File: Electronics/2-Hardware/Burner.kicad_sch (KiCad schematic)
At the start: 9 parts, among them P3 CONN_1, P6 CONN_1, Q1 Q_NMOS_DGS, U2 LM317_TO-220, U3 LM317_TO-220

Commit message: Update to KiCad
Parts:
- added D1: PMEG3010ER, Diode_SMD:Nexperia_CFP3_SOD-123W, symbol Diode:PMEG3010ER
- BT1: footprint (none) -> Battery:BatteryHolder_Keystone_1042_1x18650
- Q1: footprint (none) -> Package_TO_SOT_SMD:SOT-23
- R1: footprint ~ -> Battery:BatteryHolder_Keystone_1042_1x18650
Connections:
- net at U1.14 (5V): no longer U2.2 (VO)
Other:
- company: (none) -> Make to Innovate
- title: (none) -> HABET Burner Board - Nero
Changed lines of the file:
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@@
   (paper "A4")
   (title_block
-    (date "26 mar 2014")
+    (title "HABET Burner Board - Nero")
+    (date "2023-07-08")
+    (rev "2")
+    (company "Make to Innovate")
+    (comment 1 "Matthew E. Nelson")
   )
   (junction (at 78.74 148.59) (diameter 0) (color 0 0 0 0)
@@
   )
   (wire (pts (xy 88.9 76.2) (xy 97.79 76.2))
-    (stroke (width 0) (type default))
-  )
-  (wire (pts (xy 97.79 76.2) (xy 97.79 97.79))
     (stroke (width 0) (type default))
   )
@@
     )
     (property "Footprint" "~" (at 86.36 150.368 90)
-      (effects (font (size 0.762 0.762)))
+      (effects (font (size 0.762 0.762)) hide)
     )
     (property "Datasheet" "~" (at 86.36 148.59 0)
@@
       (effects (font (size 1.016 1.016)))
     )
-    (property "Footprint" "~" (at 52.832 161.29 90)
-      (effects (font (size 0.762 0.762)))
+    (property "Footprint" "Battery:BatteryHolder_Keystone_1042_1x18650" (at 52.832 161.29 90)
+      (effects (font (size 0.762 0.762)) hide)
     )
     (property "Datasheet" "~" (at 54.61 161.29 0)
@@
     )
     (property "Footprint" "~" (at 102.87 156.21 0)
-      (effects (font (size 1.524 1.524)))
+      (effects (font (size 1.524 1.524)) hide)
     )
     (property "Datasheet" "~" (at 102.87 156.21 0)
@@
     )
     (property "Footprint" "~" (at 102.87 161.29 0)
-      (effects (font (size 1.524 1.524)))
+      (effects (font (size 1.524 1.524)) hide)
     )
     (property "Datasheet" "~" (at 102.87 161.29 0)
@@
         (path "/ef9e4c29-e04e-4025-8830-037b9cad2048"
           (reference "P6") (unit 1)
+        )
+      )
+    )
+  )
+  (symbol (lib_id "Diode:PMEG3010ER") (at 102.87 87.63 90) (unit 1)
+    (in_bom yes) (on_board yes) (dnp no) (fields_autoplaced)
+    (property "Reference" "D1" (at 105.41 87.3125 90)
+      (effects (font (size 1.27 1.27)) (justify right))
+    )
+    (property "Value" "PMEG3010ER" (at 105.41 89.8525 90)
+      (effects (font (size 1.27 1.27)) (justify right))
+    )
+    (property "Footprint" "Diode_SMD:Nexperia_CFP3_SOD-123W" (at 107.315 87.63 0)
+      (effects (font (size 1.27 1.27)) hide)
+    )
+    (property "Datasheet" "https://assets.nexperia.com/documents/data-sheet/PMEG3010ER.pdf" (at 102.87 87.63 0)
+      (effects (font (size 1.27 1.27)) hide)
+    )
+    (pin "1")
+    (pin "2")
+    (instances
+      (project "Burner"
+        (path "/ef9e4c29-e04e-4025-8830-037b9cad2048"
+          (reference "D1") (unit 1)
         )
       )
@@
       (effects (font (size 1.27 1.27)) (justify left))
     )
-    (property "Footprint" "" (at 99.06 167.64 0)
+    (property "Footprint" "Package_TO_SOT_SMD:SOT-23" (at 99.06 167.64 0)
       (effects (font (size 1.27 1.27)) hide)
     )
@@
       (effects (font (size 1.27 1.27)) (justify left))
     )
-    (property "Footprint" "" (at 57.15 37.846 90)
-      (effects (font (size 1.27 1.27)) hide)
-    )
+    (property "Footprint" "Battery:BatteryHolder_Keystone_1042_1x18650" (at 57.15 37.846 90)
+      (effects (font (size 1.27 1.27)) hide)
+    )

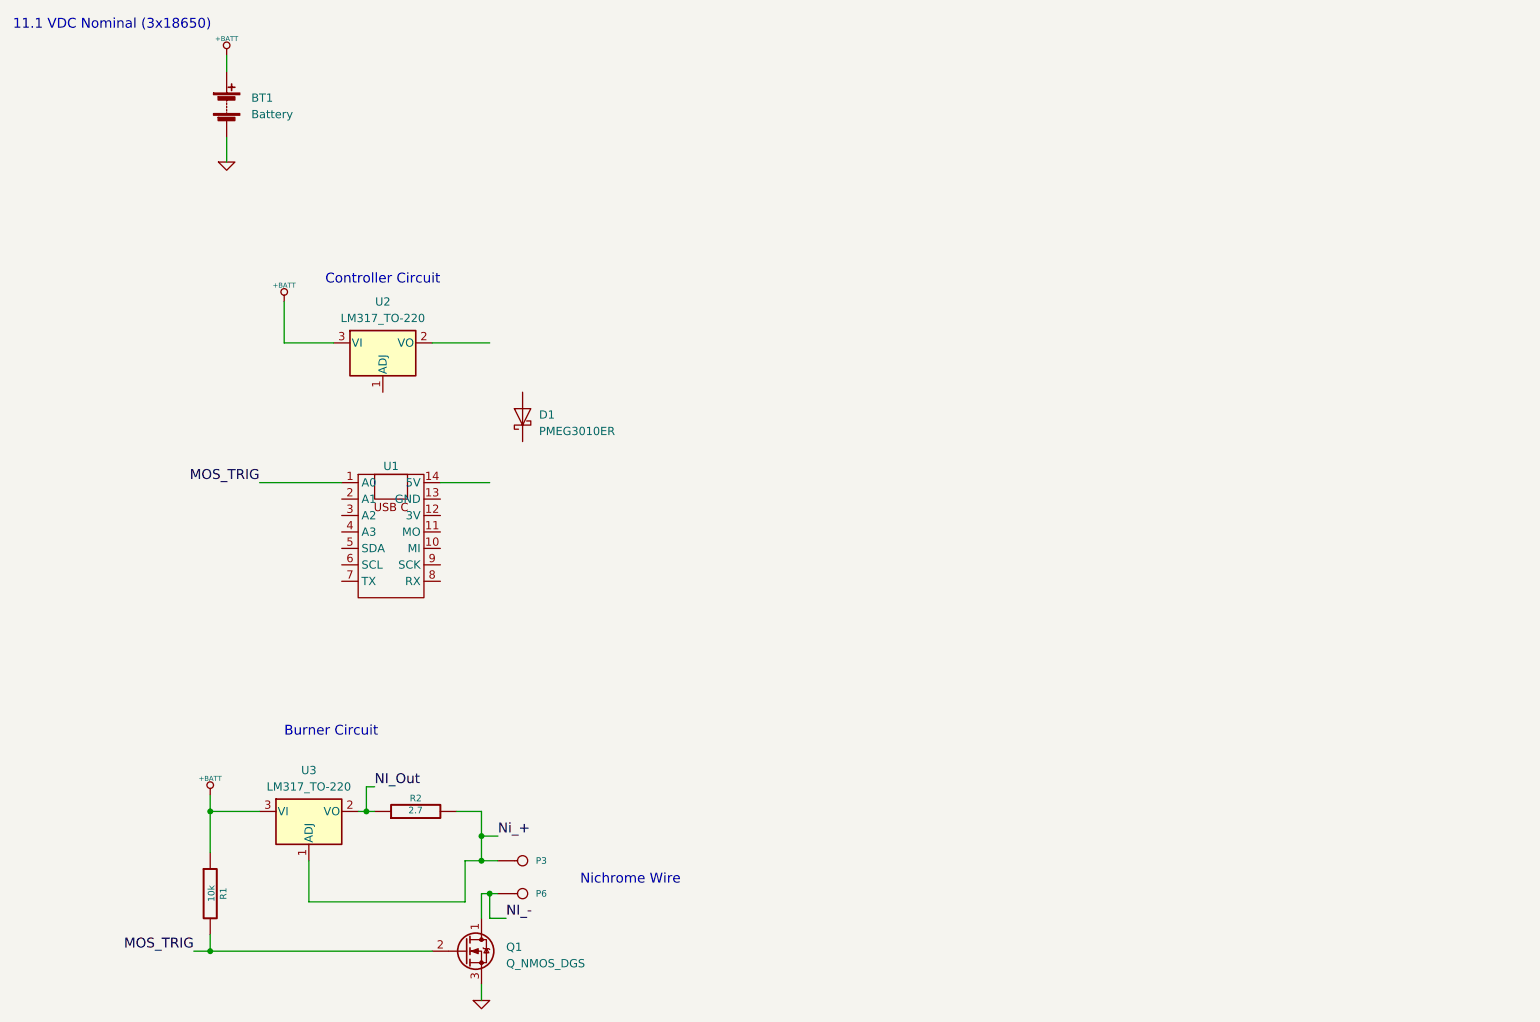
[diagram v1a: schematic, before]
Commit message: F23 update to burner
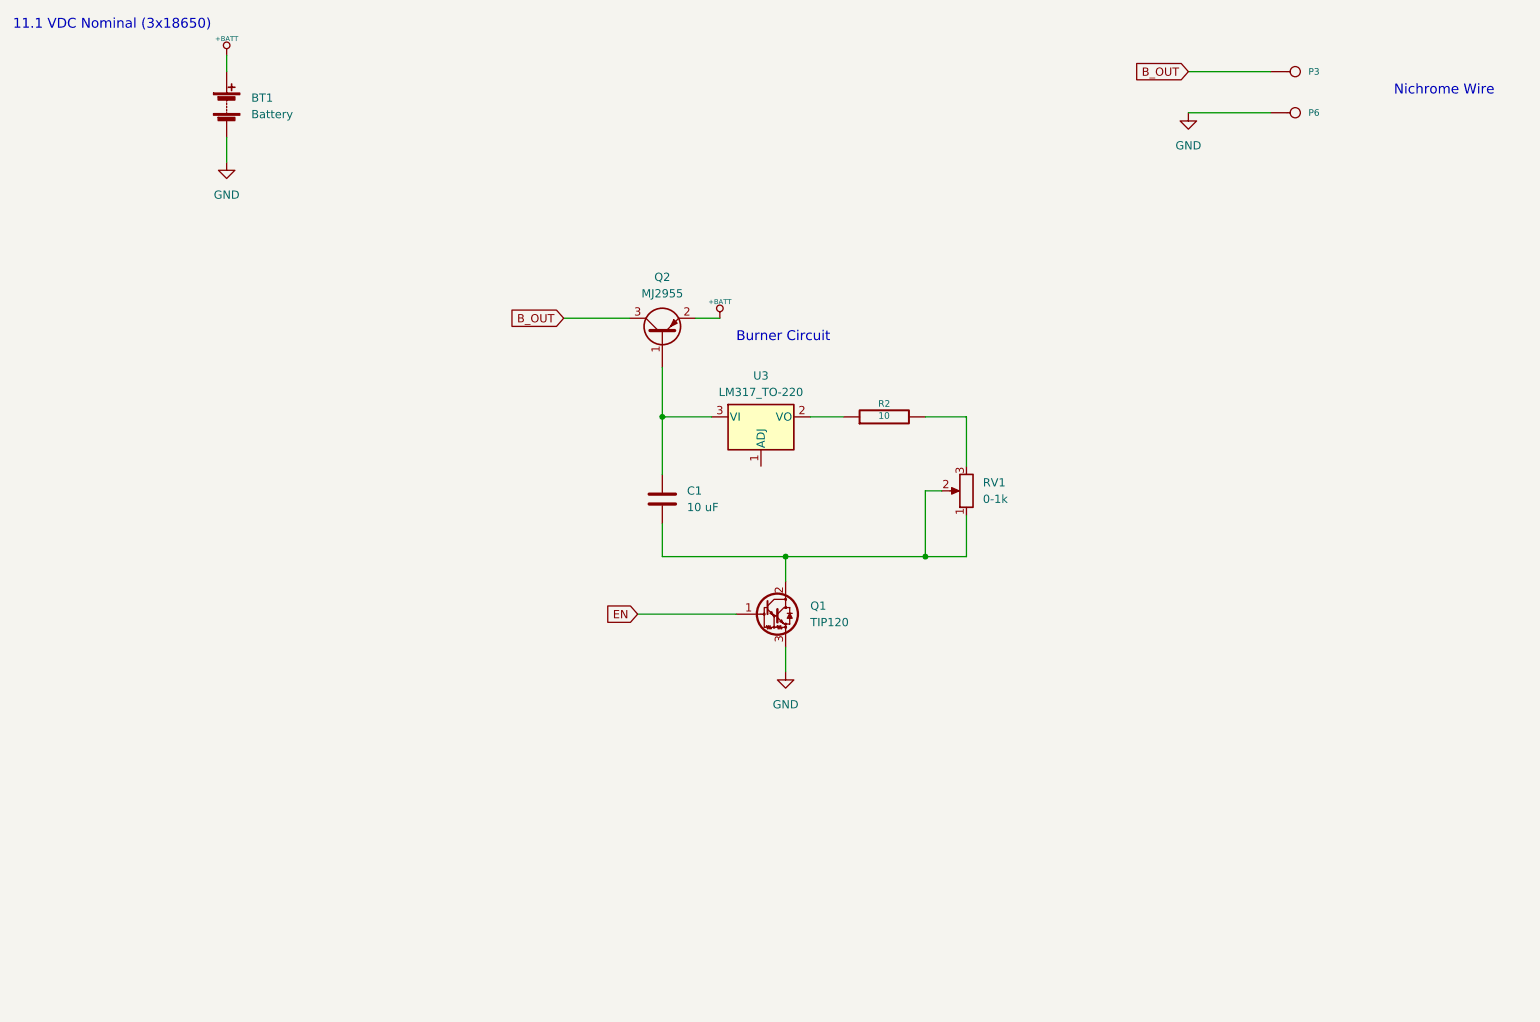
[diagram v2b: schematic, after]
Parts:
- removed D1: PMEG3010ER, Diode_SMD:Nexperia_CFP3_SOD-123W, symbol Diode:PMEG3010ER
- removed Q1: Q_NMOS_DGS, Package_TO_SOT_SMD:SOT-23, symbol Device:Q_NMOS_DGS
- removed R1: 10k, Battery:BatteryHolder_Keystone_1042_1x18650, symbol Burner-rescue:R
- removed U1: ~, symbol MCU_Espressif:QT_ESP32_S3
- removed U2: LM317_TO-220, Package_TO_SOT_THT:TO-220-3_Vertical, symbol Regulator_Linear:LM317_TO-220
- added C1: 10 uF, Capacitor_THT:CP_Axial_L10.0mm_D4.5mm_P15.00mm_Horizontal, symbol Device:C
- added Q1: TIP120, Package_TO_SOT_THT:TO-220-3_Vertical, symbol Transistor_BJT:TIP120
- added Q2: MJ2955, Package_TO_SOT_THT:TO-3, symbol Transistor_BJT:MJ2955
- added RV1: 0-1k, Potentiometer_THT:Potentiometer_Bourns_3339S_Horizontal, symbol Device:R_Potentiometer
- P3, P6: footprint ~ -> Connector_Pin:Pin_D0.7mm_L6.5mm_W1.8mm_FlatFork
- R2: value 2.7 -> 10; footprint ~ -> Resistor_THT:R_Axial_DIN0411_L9.9mm_D3.6mm_P25.40mm_Horizontal
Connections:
- net NI_- is gone; now on net GND: P6.1
- net +BATT: now also Q2.2 (E); no longer U3.3 (VI)
- net GND: now also Q1.3 (E)
- net NI_Out: no longer names the net of R2.1, U3.2 (VO)
- removed net Ni_+: P3.1, R2.2, U3.1 (ADJ)
- new net: R2.2, RV1.3
- new net: C1.2, Q1.2 (C), RV1.1, RV1.2
- new net: C1.1, Q2.1 (B), U3.3 (VI)
- new net B_OUT: P3.1, Q2.3 (C)
- new net EN: Q1.1 (B)
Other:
- note removed: "Controller Circuit"
- moved on the sheet: P3, P6, R2, U3
